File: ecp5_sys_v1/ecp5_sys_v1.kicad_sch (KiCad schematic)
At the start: 0 parts

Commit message: Brief decision on how the hierarchical schematic will look like
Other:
- added sheet CAMERA (CAMERA.kicad_sch)
- added sheet DDR (DDR.kicad_sch)
- added sheet ESP32 (ESP32.kicad_sch)
- added sheet FPGA (FPGA.kicad_sch)
- added sheet PERIPHERALS (PERIPHERALS.kicad_sch)
- added sheet POWER (POWER.kicad_sch)
- added sheet USB (USB.kicad_sch)

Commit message: Worked on USB
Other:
- sheet FPGA ports: added FPGA_JTAG{FT_OUTDATA}; removed none
- sheet USB ports: added LED_5V_TO, USB1_PU, {FT_CBUS_PROG}, {FT_OUTDATA}; removed none
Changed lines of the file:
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@@
 	(generator_version "10.0")
 	(paper "A4")
+	(bus
+		(pts
+			(xy 107.95 120.65) (xy 114.3 120.65)
+		)
+		(stroke
+			(width 0)
+			(type default)
+		)
+	)
 	(sheet
 		(at 69.85 30.48)
@@
 			)
 		)
+		(pin "LED_5V_TO" input
+			(at 107.95 106.68 0)
+			(effects
+				(font
+					(size 1.27 1.27)
+				)
+				(justify right)
+			)
+		)
+		(pin "USB1_PU" bidirectional
+			(at 107.95 110.49 0)
+			(effects
+				(font
+					(size 1.27 1.27)
+				)
+				(justify right)
+			)
+		)
+		(pin "{FT_OUTDATA}" output
+			(at 107.95 120.65 0)
+			(effects
+				(font
+					(size 1.27 1.27)
+				)
+				(justify right)
+			)
+		)
+		(pin "{FT_CBUS_PROG}" bidirectional
+			(at 107.95 115.57 0)
+			(effects
+				(font
+					(size 1.27 1.27)
+				)
+				(justify right)
+			)
+		)
 		(instances
 			(project "ecp5_sys_v1"
@@
 			)
 		)
+		(pin "FPGA_JTAG{FT_OUTDATA}" input
+			(at 114.3 120.65 180)
+			(effects
+				(font
+					(size 1.27 1.27)
+				)
+				(justify left)
+			)
+		)

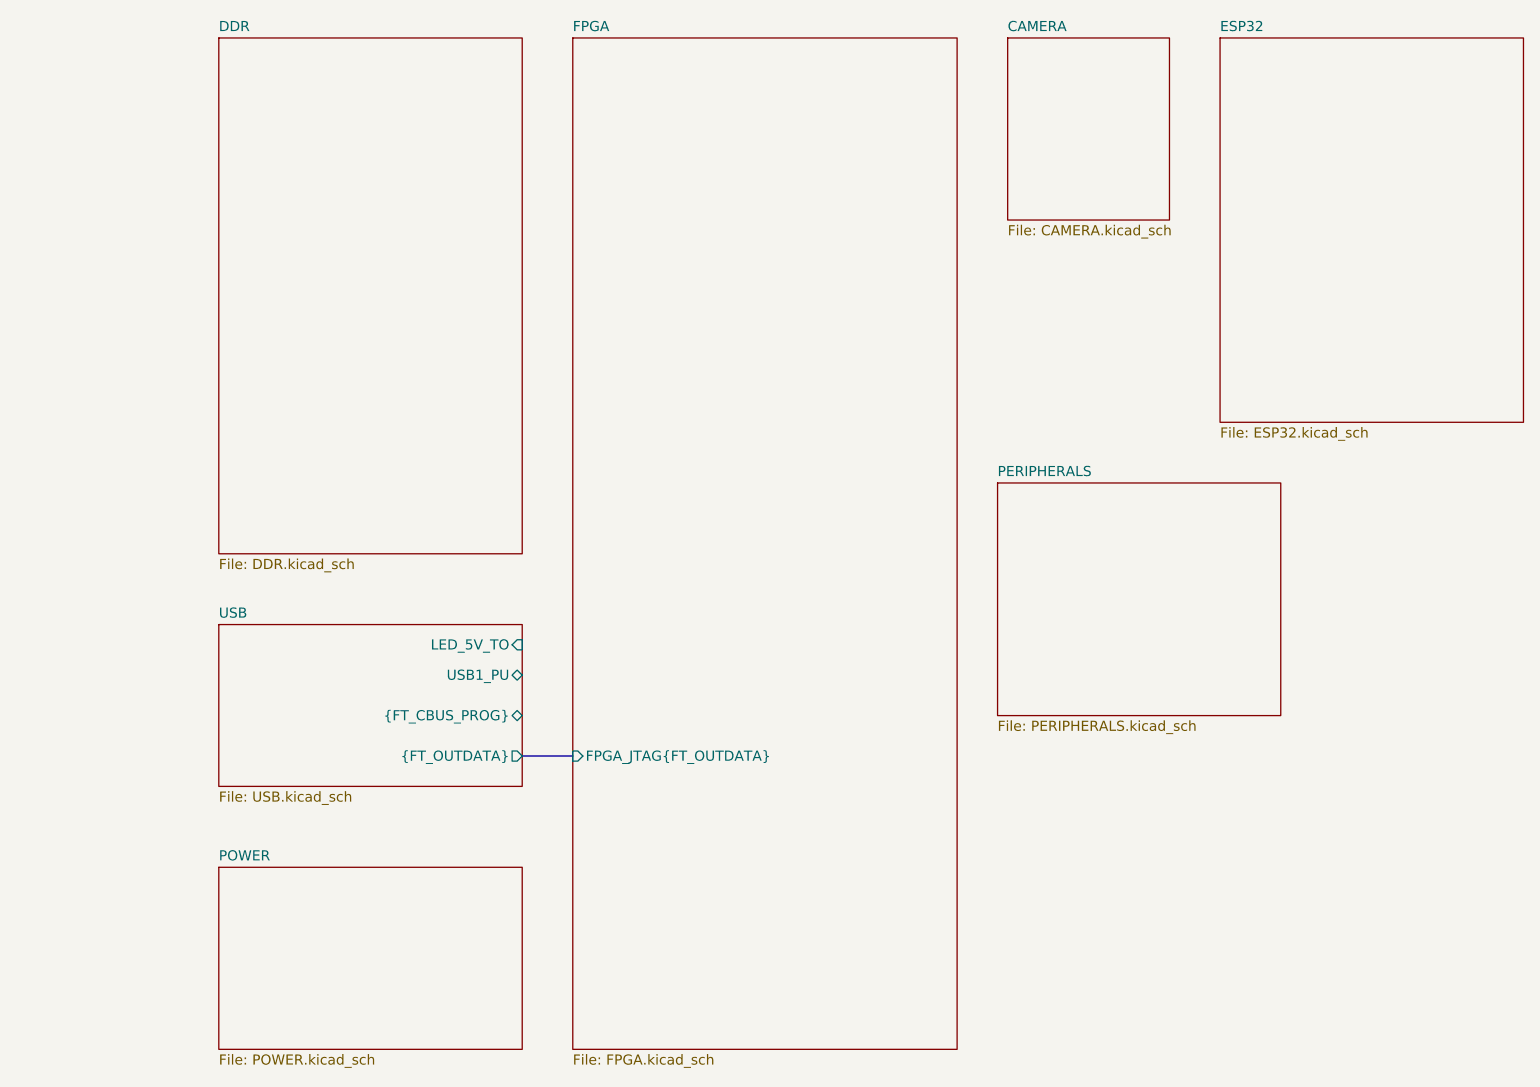
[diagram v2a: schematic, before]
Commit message: Finished USB schematic, left pins for future work and worked on ESP32, FPGA config, things have been confirmed, next up is thinking about power and how it will function into if the system is going to be just a DVP camera or also MIPI
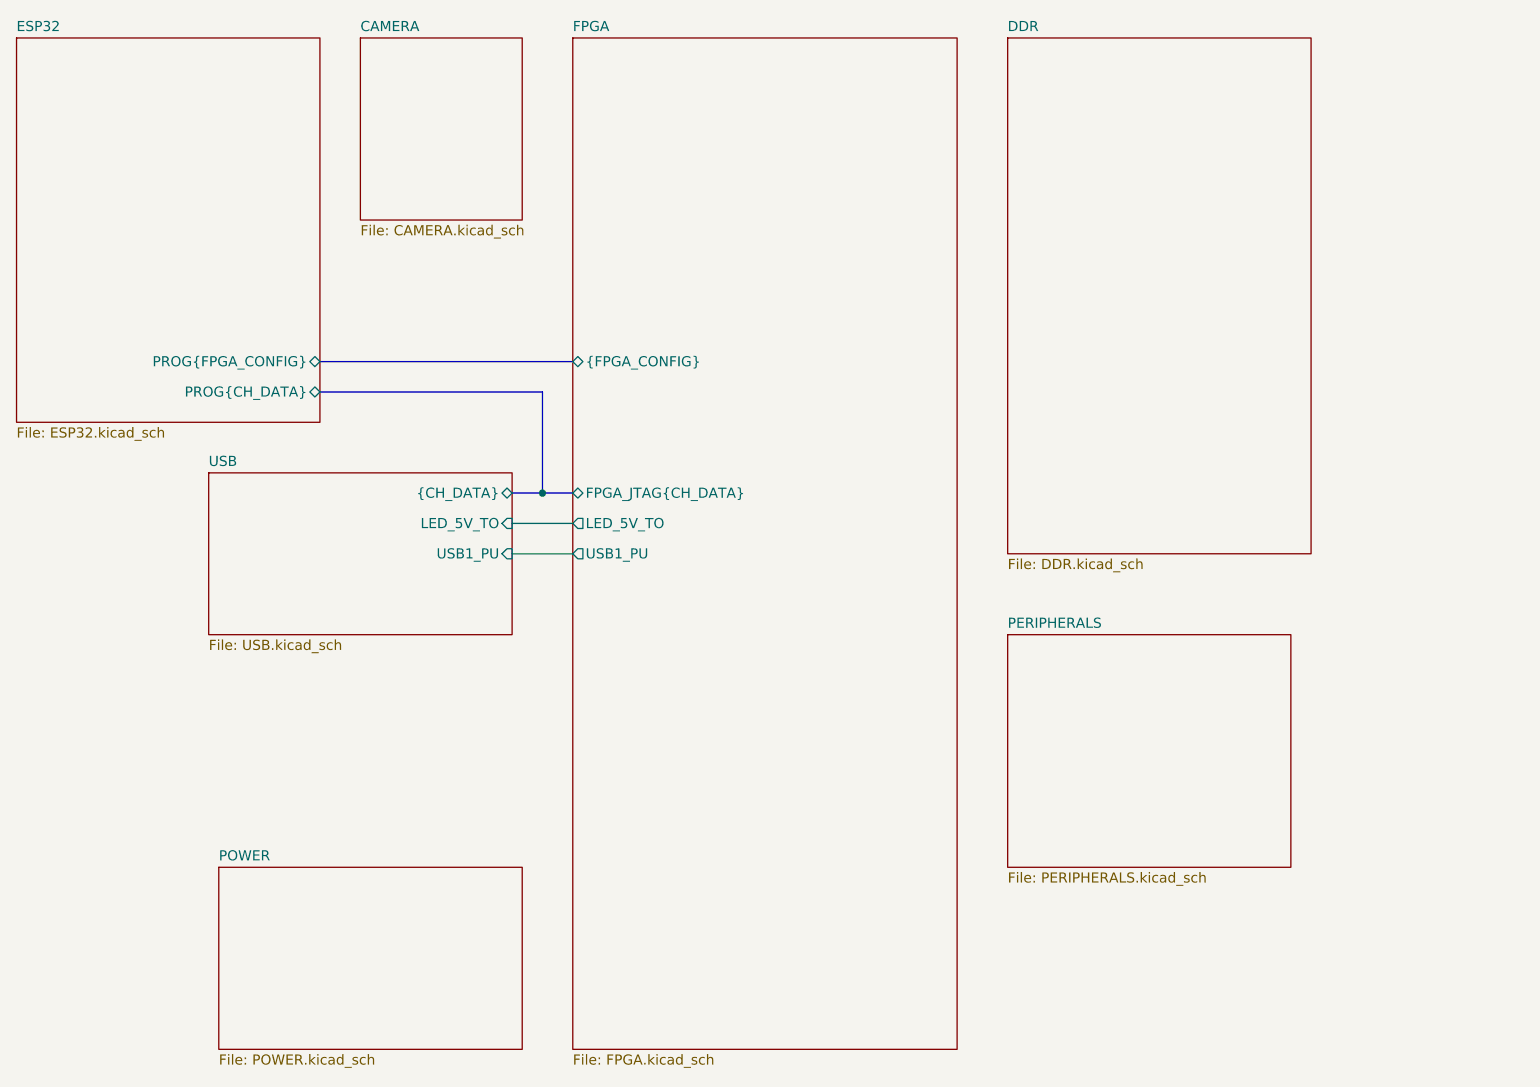
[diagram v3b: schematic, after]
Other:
- sheet ESP32 ports: added PROG{CH_DATA}, PROG{FPGA_CONFIG}; removed none
- sheet FPGA ports: added FPGA_JTAG{CH_DATA}, LED_5V_TO, USB1_PU, {FPGA_CONFIG}; removed FPGA_JTAG{FT_OUTDATA}
- sheet USB ports: added {CH_DATA}; removed {FT_CBUS_PROG}, {FT_OUTDATA}
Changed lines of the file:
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@@
 	(generator_version "10.0")
 	(paper "A4")
+	(junction
+		(at 110.49 87.63)
+		(diameter 0)
+		(color 0 0 0 0)
+	)
 	(bus
 		(pts
-			(xy 107.95 120.65) (xy 114.3 120.65)
-		)
-		(stroke
-			(width 0)
-			(type default)
-		)
-	)
-	(sheet
-		(at 69.85 30.48)
+			(xy 82.55 71.12) (xy 114.3 71.12)
+		)
+		(stroke
+			(width 0)
+			(type default)
+		)
+	)
+	(wire
+		(pts
+			(xy 106.68 95.25) (xy 114.3 95.25)
+		)
+		(stroke
+			(width 0)
+			(type default)
+		)
+	)
+	(bus
+		(pts
+			(xy 106.68 87.63) (xy 110.49 87.63)
+		)
+		(stroke
+			(width 0)
+			(type default)
+		)
+	)
+	(bus
+		(pts
+			(xy 110.49 74.93) (xy 110.49 87.63)
+		)
+		(stroke
+			(width 0)
+			(type default)
+		)
+	)
+	(bus
+		(pts
+			(xy 110.49 87.63) (xy 114.3 87.63)
+		)
+		(stroke
+			(width 0)
+			(type default)
+		)
+	)
+	(wire
+		(pts
+			(xy 106.68 91.44) (xy 114.3 91.44)
+		)
+		(stroke
+			(width 0)
+			(type default)
+		)
+	)
+	(bus
+		(pts
+			(xy 82.55 74.93) (xy 110.49 74.93)
+		)
+		(stroke
+			(width 0)
+			(type default)
+		)
+	)
+	(sheet
+		(at 168.91 30.48)
 		(size 38.1 64.77)
 		(exclude_from_sim no)
@@
 		)
 		(property "Sheetname" "DDR"
-			(at 69.85 29.7684 0)
+			(at 168.91 29.7684 0)
 			(show_name no)
 			(do_not_autoplace no)
@@
 		)
 		(property "Sheetfile" "DDR.kicad_sch"
-			(at 69.85 95.8346 0)
+			(at 168.91 95.8346 0)
 			(show_name no)
 			(do_not_autoplace no)
@@
 	)
 	(sheet
-		(at 167.64 86.36)
+		(at 168.91 105.41)
 		(size 35.56 29.21)
 		(exclude_from_sim no)
@@
 		)
 		(property "Sheetname" "PERIPHERALS"
-			(at 167.64 85.6484 0)
+			(at 168.91 104.6984 0)
 			(show_name no)
 			(do_not_autoplace no)
@@
 		)
 		(property "Sheetfile" "PERIPHERALS.kicad_sch"
-			(at 167.64 116.1546 0)
+			(at 168.91 135.2046 0)
 			(show_name no)
 			(do_not_autoplace no)
@@
 	)
 	(sheet
-		(at 168.91 30.48)
+		(at 87.63 30.48)
 		(size 20.32 22.86)
 		(exclude_from_sim no)
@@
 		)
 		(property "Sheetname" "CAMERA"
-			(at 168.91 29.7684 0)
+			(at 87.63 29.7684 0)
 			(show_name no)
 			(do_not_autoplace no)
@@
 		)
 		(property "Sheetfile" "CAMERA.kicad_sch"
-			(at 168.91 53.9246 0)
+			(at 87.63 53.9246 0)
 			(show_name no)
 			(do_not_autoplace no)
@@
 	)
 	(sheet
-		(at 69.85 104.14)
+		(at 68.58 85.09)
 		(size 38.1 20.32)
 		(exclude_from_sim no)
@@
 		)
 		(property "Sheetname" "USB"
-			(at 69.85 103.4284 0)
+			(at 68.58 84.3784 0)
 			(show_name no)
 			(do_not_autoplace no)
@@
 		)
 		(property "Sheetfile" "USB.kicad_sch"
-			(at 69.85 125.0446 0)
+			(at 68.58 105.9946 0)
 			(show_name no)
 			(do_not_autoplace no)
@@
 		)
 		(pin "LED_5V_TO" input
-			(at 107.95 106.68 0)
+			(at 106.68 91.44 0)
 			(effects
 				(font
@@
 			)
 		)
-		(pin "USB1_PU" bidirectional
-			(at 107.95 110.49 0)
+		(pin "USB1_PU" input
+			(at 106.68 95.25 0)
 			(effects
 				(font
@@
 			)
 		)
-		(pin "{FT_OUTDATA}" output
-			(at 107.95 120.65 0)
+		(pin "{CH_DATA}" bidirectional
+			(at 106.68 87.63 0)
 			(effects
 				(font
@@
 			)
 		)
-		(pin "{FT_CBUS_PROG}" bidirectional
-			(at 107.95 115.57 0)
+		(instances
+			(project "ecp5_sys_v1"
+				(path "/08f8cf6b-931b-453e-b2e0-0373288a9134"
+					(page "6")
+				)
+			)
+		)
+	)
+	(sheet
+		(at 44.45 30.48)
+		(size 38.1 48.26)
+		(exclude_from_sim no)
+		(in_bom yes)
+		(on_board yes)
+		(dnp no)
+		(fields_autoplaced yes)
+		(stroke
+			(width 0.1524)
+			(type solid)
+		)
+		(fill
+			(color 0 0 0 0)
+		)
+		(property "Sheetname" "ESP32"
+			(at 44.45 29.7684 0)
+			(show_name no)
+			(do_not_autoplace no)
+			(effects
+				(font
+					(size 1.27 1.27)
+				)
+				(justify left bottom)
+			)
+		)
+		(property "Sheetfile" "ESP32.kicad_sch"
+			(at 44.45 79.3246 0)
+			(show_name no)
+			(do_not_autoplace no)
+			(effects
+				(font
+					(size 1.27 1.27)
+				)
+				(justify left top)
+			)
+		)
+		(pin "PROG{CH_DATA}" bidirectional
+			(at 82.55 74.93 0)
 			(effects
 				(font
@@
 			)
 		)
-		(instances
-			(project "ecp5_sys_v1"
-				(path "/08f8cf6b-931b-453e-b2e0-0373288a9134"
-					(page "6")
-				)
-			)
-		)
-	)
-	(sheet
-		(at 195.58 30.48)
-		(size 38.1 48.26)
-		(exclude_from_sim no)
-		(in_bom yes)
-		(on_board yes)
-		(dnp no)
-		(fields_autoplaced yes)
-		(stroke
-			(width 0.1524)
-			(type solid)
-		)
-		(fill
-			(color 0 0 0 0)
-		)
-		(property "Sheetname" "ESP32"
-			(at 195.58 29.7684 0)
-			(show_name no)
-			(do_not_autoplace no)
-			(effects
-				(font
-					(size 1.27 1.27)
-				)
-				(justify left bottom)
-			)
-		)
-		(property "Sheetfile" "ESP32.kicad_sch"
-			(at 195.58 79.3246 0)
-			(show_name no)
-			(do_not_autoplace no)
-			(effects
-				(font
-					(size 1.27 1.27)
-				)
-				(justify left top)
+		(pin "PROG{FPGA_CONFIG}" bidirectional
+			(at 82.55 71.12 0)
+			(effects
+				(font
+					(size 1.27 1.27)
+				)
+				(justify right)
 			)
 		)
@@
 			)
 		)
-		(pin "FPGA_JTAG{FT_OUTDATA}" input
-			(at 114.3 120.65 180)
-			(effects
-				(font
+		(pin "FPGA_JTAG{CH_DATA}" bidirectional
+			(at 114.3 87.63 180)
+			(effects
+				(font
+					(size 1.27 1.27)
+				)
+				(justify left)
+			)
+		)
+		(pin "{FPGA_CONFIG}" bidirectional
+			(at 114.3 71.12 180)
+			(effects
+				(font
+					(size 1.27 1.27)
+				)
+				(justify left)
+			)
+		)
+		(pin "LED_5V_TO" output
+			(at 114.3 91.44 180)
+			(effects
+				(font
+					(size 1.27 1.27)
+				)
+				(justify left)
+			)
+		)
+		(pin "USB1_PU" output
+			(at 114.3 95.25 180)
+			(effects
+				(font
